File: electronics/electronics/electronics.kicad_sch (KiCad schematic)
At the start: 21 parts, among them U1 TL074, U2 TL074, U3 TL074, U4 TL074

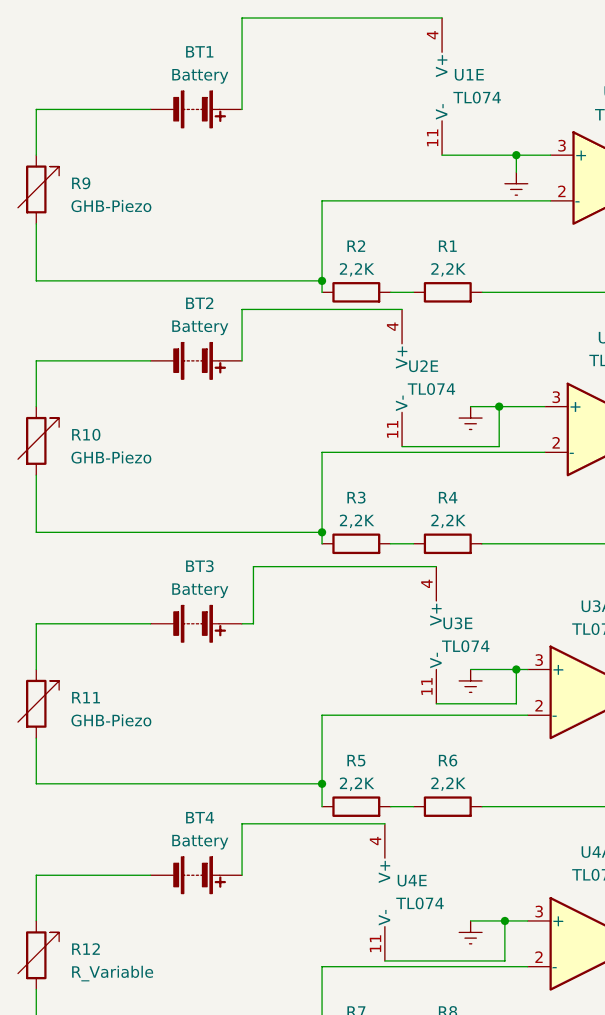
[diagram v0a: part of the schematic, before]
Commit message: Found SPICE models for simulation of the circuit with TL074 opamps. Will check if we can find simulation models for TL071 opamps.
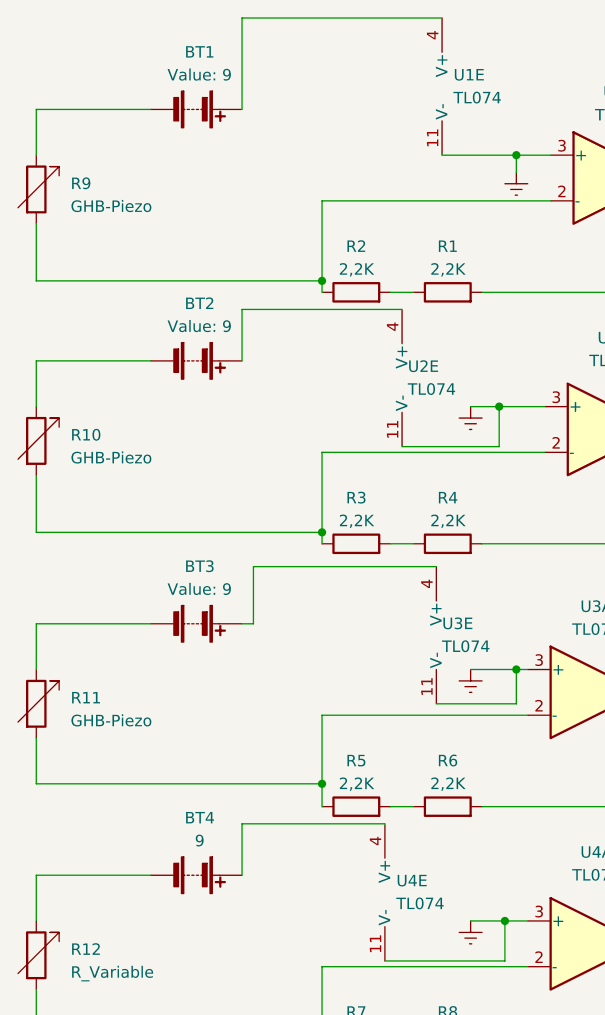
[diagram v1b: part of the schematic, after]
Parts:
- BT1, BT2, BT3, BT4: value Battery -> 9
- TTGO1: footprint ttgo-tdisplay-kicad-master:TTGO_ESP32_TDisplay_v1.1 -> ESP32_TTGO:TTGO_ESP32_TDisplay_v1.1
- U1, U2, U3, U4: footprint (none) -> Package_DIP:DIP-14_W7.62mm_LongPads
